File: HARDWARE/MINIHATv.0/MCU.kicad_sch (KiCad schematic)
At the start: 54 parts, among them P1 USB_C_Plug_USB2.0, SW1 SW_Push, U2 STM32H747IGTx, U3 CP2102N-Axx-xQFN28

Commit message: editorial changes
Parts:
- removed C3: 4u7, symbol Device:C_Small_US
- removed C4: 100n, symbol Device:C_Small
- removed C5: 1u, symbol Device:C_Small
- removed D4, D5: SP0503BAHT, symbol Device:D_Zener
- removed P1: USB_C_Plug_USB2.0, symbol Connector:USB_C_Plug_USB2.0
- removed R4, R5: 100, symbol Device:R
- removed SW1: SW_Push, Button_Switch_SMD:SW_Push_1P1T_NO_CK_KMR2, symbol Switch:SW_Push
- removed U3: CP2102N-Axx-xQFN28, Package_DFN_QFN:QFN-28-1EP_5x5mm_P0.5mm_EP3.35x3.35mm, symbol Interface_USB:CP2102N-Axx-xQFN28
- added R46, R48, R53, R58, R65, R66: 33, symbol Device:R
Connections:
- net BA0: now also R46.1
- net DEBUG_RX: no longer U2.87 (PB14), U3.25 (RXD)
- net GND: now also U2.100 (VSS), U2.105 (VSSDSI), U2.109 (VSSDSI), U2.112 (VSS), U2.119 (VSS), U2.12 (VSS), U2.134 (VSS), U2.137 (VSS), U2.14 (VSSSMPS), U2.151 (VSS), U2.159 (VSS), U2.173 (VSS), U2.24 (VSS), U2.38 (VSSA), U2.45 (VSS), U2.47 (VSS), U2.6 (VSS), U2.64 (VSS), U2.70 (VSS), U2.81 (VSS), U2.83 (VSS), U2.93 (VSS)
- net NBL1: now also R62.1
- net QSPI.CLK: now also U2.57 (PB2)
- net QSPI.D0: now also U2.28 (PF8)
- net QSPI.D3: now also U2.26 (PF6)
- net RMII.CRS_DV: now also U2.52 (PA7)
- net RMII.MDIO: now also U2.43 (PA2)
- net RMII.RXD0: now also U2.53 (PC4)
- net RMII.TXD0: now also U2.156 (PG12)
- net RMII.TXD1: now also U2.157 (PG13)
- net RMII.TXDEN: now also U2.155 (PG11)
- net SDCLK: now also R48.1
- net SDIO.CLK: now also U2.142 (PC12)
- net SDIO.CMD: now also U2.145 (PD2)
- net SDIO.DAT1: now also U2.125 (PC9)
- net SDNCAS: now also R49.1
- net SDNEO: now also R73.2
- net SDRAM_ADDR1: now also R51.1
- net SDRAM_ADDR2: now also R52.1
- net SDRAM_ADDR3: now also R53.1
- net SDRAM_ADDR5: now also R55.1
- net SDRAM_DATA1: now also R81.2
- net SDRAM_DATA10: now also R69.1
- net SDRAM_DATA12: now also R71.1
- net SDRAM_DATA15: now also R79.2
- net SDRAM_DATA2: now also R75.2
- net SDRAM_DATA6: now also R65.1
- net SDRAM_DATA8: now also R67.1
- net USB_N: now also U2.130 (PA11)
- net USB_P: now also U2.131 (PA12)
- net USB_SENSE: now also U2.128 (PA9)
- net at R80.1: now also U2.97 (PD14)
- net SDRAM_DATA0: now reaches R80.2
- net at R77.1: now also U2.89 (PD8)
- net SDRAM_DATA9: now reaches R68.1
- net at U2.114 (PG4): now also R46.2
- net at U2.115 (PG5): now also R47.2
- net at U2.118 (PG8): now also R48.2
- net SDIO.DAT3: now reaches U2.141 (PC11)
- net at U2.171 (PE1): now also R62.2
- net at U2.20 (PF2): now also R52.2
- net at U2.21 (PF3): now also R53.2
- net QSPI.D2: now reaches U2.27 (PF7)
- net RMII.RXD1: now reaches U2.54 (PC5)
- net at U2.60 (PF13): now also R58.2
- net at U2.69 (PE9): now also R65.2
- net at U2.72 (PE10): now also R66.2
- net at U2.76 (PE14): now also R70.2
- net SDRAM_ADDR9: now reaches R60.1
- net SDRAM_DATA4: now reaches R63.1
- net at R67.2: now also U2.73 (PE11)
- net SDRAM_ADDR10: now reaches R44.1
- net SDRAM_DATA5: now reaches R64.1
- net SDRAM_DATA3: now reaches R76.2
- net BT_RX: no longer names the net of U2.149 (PD6)
- net BT_TX: no longer names the net of U2.148 (PD5)
- net HDMI_SDA renamed QSPI.CS
- net LTDC_B3: no longer names the net of R79.1, U2.91 (PD10)
- net LTDC_B4: no longer names the net of R68.2, U2.74 (PE12)
- net LTDC_B5: no longer names the net of U2.46 (PA3)
- net LTDC_CEC: no longer names the net of U2.139 (PA15)
- net LTDC_DE: no longer names the net of U2.30 (PF10)
- net LTDC_G2: no longer names the net of U2.51 (PA6)
- removed net LTDC_G3: R67.1, U2.73 (PE11)
- net LTDC_G4: no longer names the net of U2.78 (PB10)
- net LTDC_G5: no longer names the net of U2.79 (PB11)
- net LTDC_R5: no longer names the net of R72.1, U2.34 (PC0)
- net LTDC_R6: no longer names the net of U2.56 (PB1)
- net LTDC_R7: no longer names the net of R71.2, U2.77 (PE15)
- net LTDC_VSYNC: no longer names the net of U2.49 (PA4)
- net {MCU_LTDC_BUS} renamed QSPI.D1
- net QSPI.D1: no longer R78.2
- new net DEBUG_TX: U2.87 (PB14), U3.25 (RXD)
- new net SDRAM_ADDR7: R58.1
- new net SDRAM_DATA14: R78.2
- new net SDRAM_DATA7: R66.1

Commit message: added sdram and usb pages to top page
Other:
- moved on the sheet: C3, C4, C5, C6, D3, D4, D5, P1, R6, SW1, U3

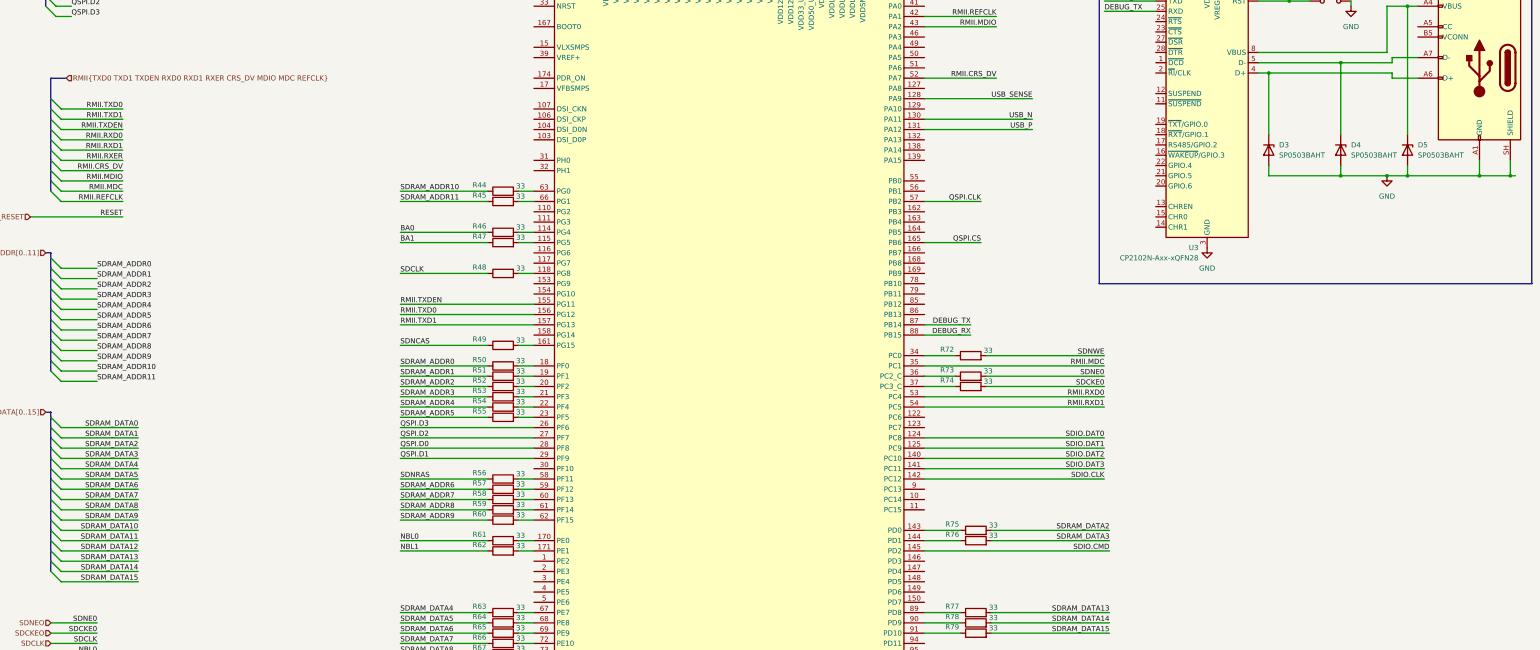
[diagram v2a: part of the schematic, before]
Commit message: added ltdc bus to mcu page, editoral change to rmii bus
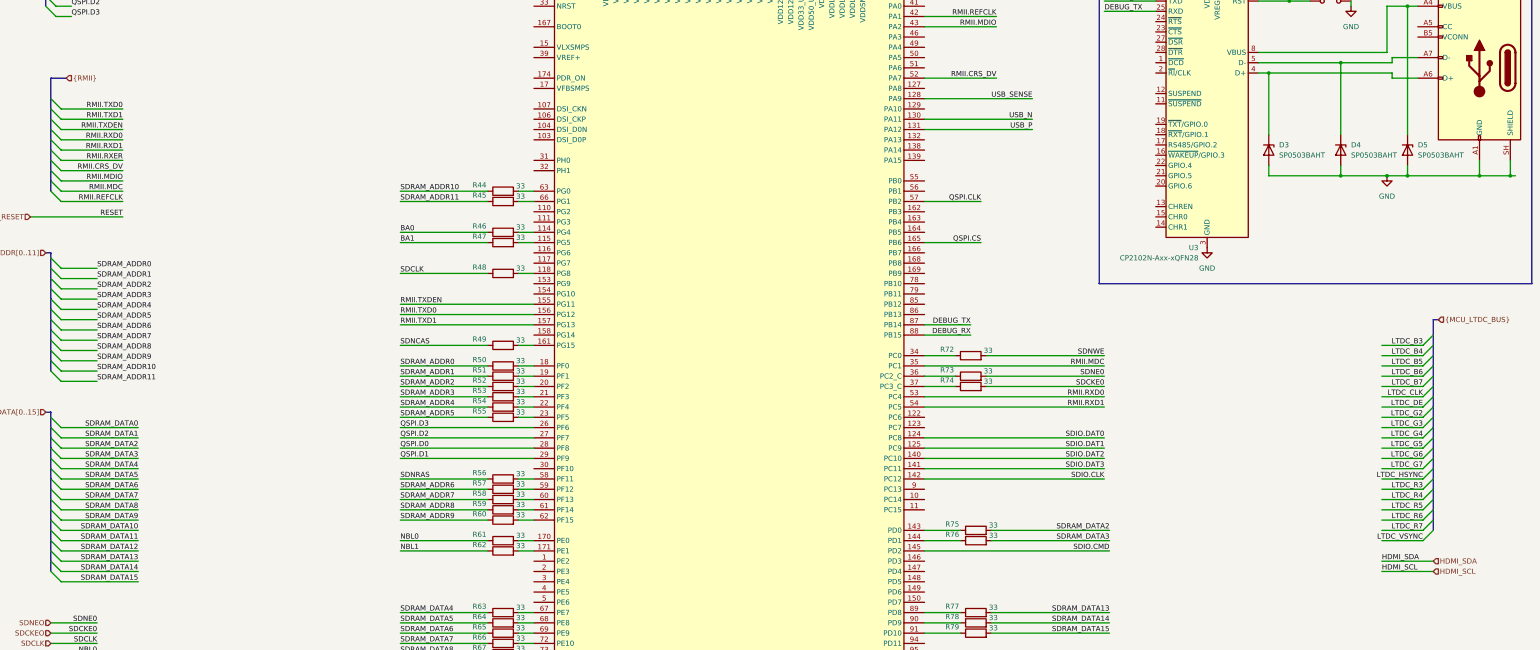
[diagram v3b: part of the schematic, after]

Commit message: connecting i2c and uart bt/hdmi
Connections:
- net HDMI_SCL: now also U2.95 (PD12)
- net HDMI_SDA: now also U2.96 (PD13)
- net LTDC_B4: now also U2.127 (PA8)
- net LTDC_B5: now also U2.129 (PA10)
- net LTDC_B6: now also U2.46 (PA3)
- net LTDC_B7: now also U2.168 (PB8)
- net LTDC_CLK: now also U2.169 (PB9)
- net LTDC_DE: now also U2.117 (PG7)
- net LTDC_G2: now also U2.30 (PF10)
- net LTDC_G3: now also U2.51 (PA6)
- net LTDC_G4: now also U2.154 (PG10)
- net LTDC_G5: now also U2.79 (PB11)
- net LTDC_G6: now also U2.123 (PC7)
- net LTDC_G7: now also U2.146 (PD3)
- net LTDC_HSYNC: now also U2.122 (PC6)
- net LTDC_R3: now also U2.55 (PB0)
- net LTDC_R4: now also U2.50 (PA5)
- net LTDC_R5: now also U2.128 (PA9)
- net LTDC_R6: now also U2.56 (PB1)
- net LTDC_R7: now also U2.116 (PG6)
- net LTDC_VSYNC: now also U2.49 (PA4)
- net USB_SENSE: no longer U2.128 (PA9)
- net BT_RX: now reaches U2.139 (PA15)
- net BT_TX: now reaches U2.162 (PB3)
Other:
- note added: "I2C4"
- note added: "UART7"
- note added: "USART1"
- moved on the sheet: R44, R45, R46, R47, R48, R49, R50, R51, R52, R53, R54, R55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

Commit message: mcu pwr/vcap ports, hdmi gpio, buses
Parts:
- added C61, C63: 10u, Capacitor_SMD:C_1206_3216Metric_Pad1.33x1.80mm_HandSolder, symbol Device:C_Small_US
- added C62, C64, C80: 100n, Capacitor_SMD:C_1206_3216Metric_Pad1.33x1.80mm_HandSolder, symbol Device:C_Small
- added C65, C66, C67, C68, C69, C70, C71, C72, C73, C74, C75, C76, C77, C78, C81, C82, C83, C84, C85, C86: 100n, symbol Device:C_Small
- added C79: 100n, Capacitor_SMD:C_0603_1608Metric_Pad1.08x0.95mm_HandSolder, symbol Device:C
- added C87, C88, C89: 2,2u, symbol Device:C_Small
- added FB5: BLM18AG121SN1, Inductor_SMD:L_0603_1608Metric_Pad1.05x0.95mm_HandSolder, symbol Device:FerriteBead
- added J7: Conn_01x02, Connector_PinHeader_2.54mm:PinHeader_1x02_P2.54mm_Vertical, symbol Connector_Generic:Conn_01x02
- added JP1: Jumper_2_Small_Bridged, Jumper:SolderJumper-2_P1.3mm_Bridged_RoundedPad1.0x1.5mm, symbol Jumper:Jumper_2_Small_Bridged
- added R84: 1k, Resistor_SMD:R_0603_1608Metric_Pad0.98x0.95mm_HandSolder, symbol Device:R_Small
- added R85: 4k7, Resistor_SMD:R_0603_1608Metric_Pad0.98x0.95mm_HandSolder, symbol Device:R_Small
- added R86, R87: 10k, Resistor_SMD:R_0603_1608Metric_Pad0.98x0.95mm_HandSolder, symbol Device:R_Small
- added R88: 510k, Resistor_SMD:R_0603_1608Metric_Pad0.98x0.95mm_HandSolder, symbol Device:R_Small
- added SW4: SW_Push, Button_Switch_SMD:SW_Push_1P1T_NO_CK_KMR2, symbol Switch:SW_Push
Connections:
- net GND is gone; now on net +3V3: C3.1, C4.1, C5.2, C6.2, D3.2 (A), D4.2 (A), D5.2 (A), P1.A1 (GND), P1.A12 (GND), P1.B1 (GND), P1.B12 (GND), P1.SH (SHIELD), SW1.2, U2.100 (VSS), U2.105 (VSSDSI), U2.109 (VSSDSI), U2.112 (VSS), U2.119 (VSS), U2.12 (VSS), U2.134 (VSS), U2.137 (VSS), U2.14 (VSSSMPS), U2.151 (VSS), U2.159 (VSS), U2.173 (VSS), U2.24 (VSS), U2.38 (VSSA), U2.45 (VSS), U2.47 (VSS), U2.6 (VSS), U2.64 (VSS), U2.70 (VSS), U2.81 (VSS), U2.83 (VSS), U2.93 (VSS), U3.29 (GND), U3.3 (GND)
- net +3V3: now also U2.113 (VDD), U2.126 (VDD), U2.13 (VDD), U2.133 (VCAP), U2.135 (VDDLDO), U2.136 (VDD), U2.152 (VDD), U2.160 (VDD), U2.172 (VCAP), U2.175 (VDDLDO), U2.176 (VDD), U2.25 (VDD), U2.44 (VDD), U2.48 (VDD), U2.65 (VDD), U2.7 (VDD), U2.71 (VDD), U2.80 (VCAP), U2.82 (VDDLDO), U2.84 (VDD), U2.92 (VDD), U2.99 (VDD), C61.1, C61.2, C62.1, C62.2, C65.1, C65.2, C66.1, C66.2, C67.1, C67.2, C68.1, C68.2, C69.1, C69.2, C70.1, C70.2, C71.1, C71.2, C72.1, C72.2, C73.1, C73.2, C74.1, C74.2, C75.1, C75.2, C76.1, C76.2, C77.1, C77.2, C78.1, C78.2, C79.2, C80.2, C81.1, C81.2, C82.1, C82.2, C83.1, C83.2, C84.1, C84.2, C85.1, C85.2, C86.1, C86.2, C87.1, C87.2, C88.1, C88.2, C89.1, C89.2, FB5.1, JP1.1 (A), R84.2, R85.1, R86.2, R88.2
- net BT_RX: now also U2.163 (PB4); no longer U2.139 (PA15)
- net MCU_LTDC_CEC: now reaches U2.138 (PA14)
- net BOOT: now reaches U2.167 (BOOT0)
- net BOOT: now also C80.1, R87.1, R88.1
- net NRST: now reaches U2.33 (NRST)
- net NRST: now also C79.1, R85.2, SW4.2
- net VDDA: now reaches U2.40 (VDDA)
- net VDDA: now also C63.1, C64.1, FB5.2
- new net: R84.1, SW4.1
- new net: J7.1 (Pin_1), R86.1
- new net: J7.2 (Pin_2), R87.2
- new net AGND: C63.2, C64.2, JP1.2 (B)
- new net LTDC_CEC: U2.139 (PA15)
- no-connect marks 0 -> 7
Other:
- moved on the sheet: R44, R45, R46, R47, R48, R49, R50, R51, R52, R53, R54, R55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

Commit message: audio page added to top
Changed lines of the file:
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@@
+		)
+	)
+	(hierarchical_label "I2S{CLK DIN DOUT WS}"
+		(shape input)
+		(at 314.96 127 0)
+		(effects
+			(font
+				(size 1.27 1.27)
+			)
+			(justify left)
 		)
 	)

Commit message: BT 1V2 lowdrop added, fdcan pinned to mcu, usb status led added
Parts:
- added D10, D8, D9: LED, symbol Device:LED
- added J9: Conn_01x02, symbol Connector_Generic:Conn_01x02
- added R91, R92, R93: 220, symbol Device:R_Small
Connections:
- net +3V3: now also D10.1 (K), D8.1 (K), D9.1 (K)
- net DEBUG_RX: now also J9.1 (Pin_1)
- net DEBUG_TX: now also J9.2 (Pin_2)
- net at U2.2 (PE3): now also R91.2
- net at U2.3 (PE4): now also R92.2
- net at U2.4 (PE5): now also R93.2
- net FDCAN_Tx: now reaches U2.85 (PB12)
- net FDCAN_Rx: now reaches U2.86 (PB13)
- new net: D10.2 (A), R93.1
- new net: D8.2 (A), R91.1
- new net: D9.2 (A), R92.1
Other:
- moved on the sheet: SW1
